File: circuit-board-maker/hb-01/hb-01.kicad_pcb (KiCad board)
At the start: 2 copper layers, 48 x 40 mm, 0 parts

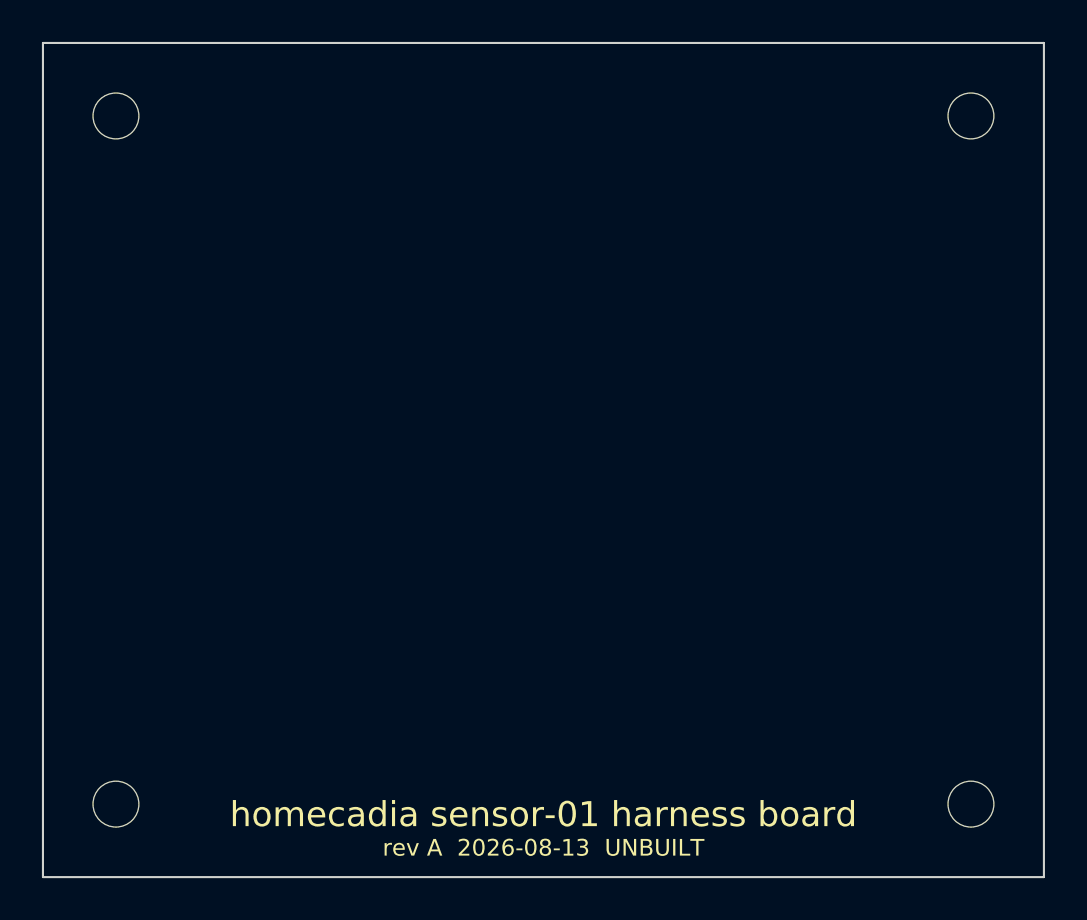
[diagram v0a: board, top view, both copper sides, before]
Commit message: fix(pcb): validate both boards against KiCad 10, place footprints, fix real errors
Ran the generated files through the Windows KiCad 10.0.5 install via
kicad-cli from WSL. This turned the boards from unvalidated text into
something KiCad parses, places, DRCs and renders - and caught six real
errors in the process.

Verified:
- all 13 footprint library refs resolve against KiCad 10's libraries
- kicad-cli pcb upgrade accepts both boards
- 26 footprints place with nets assigned, 0 missing
- J1's 17 pads are byte-identical to the library after round-trip
- both boards render in 3D (img/*-render.png are kicad-cli output)
- sb-01 passes DRC with 0 errors
- encoder terminals checked against the Bourns PEC11R datasheet:
  5x dia-1.0mm holes, 2.5mm pitch, 5.0mm spans - footprint matches

Fixed:
- Sensirion_DFN-4-1EP_1.5x1.5mm_P0.8mm_EP0.7x0.9mm does not exist. The
  real footprint is Sensirion_DFN-4_1.5x1.5mm_P0.8mm_SHT4x_NoCentralPad
- encoder moved from the Alps EC11E footprint to Bourns
  PEC12R-3x17F-Sxxxx; identical pad coordinates but 3.1mm oval boss
  holes instead of 2.8mm round, which is the safer error direction
- USB-C on hb-01 and JST-SH on sb-01 both hung off the board edge
- sb-01 C1 and J1 collided; board grown 12x12 -> 14x16 and reprovisioned
- sb-01 silkscreen overflowed the board outline
- D+/D- were documented as broken out to test pads but never netted;
  they now go to TP5/TP6

Not resolved, documented in README: hb-01 reports 65 DRC errors, all 65
inside J1 and none anywhere else. The XKB USB-C land pattern has 0.2mm
pad gaps and kicad-cli falls back to KiCad's default 0.2mm clearance
because this hand-written .kicad_pro is too minimal to load rules from -
setting the netclass to 0.05mm changed nothing. Needs one pass through
Board Setup in the GUI. That is where these generator scripts stop.

Also gitignores .kicad_prl, which is per-user local state.
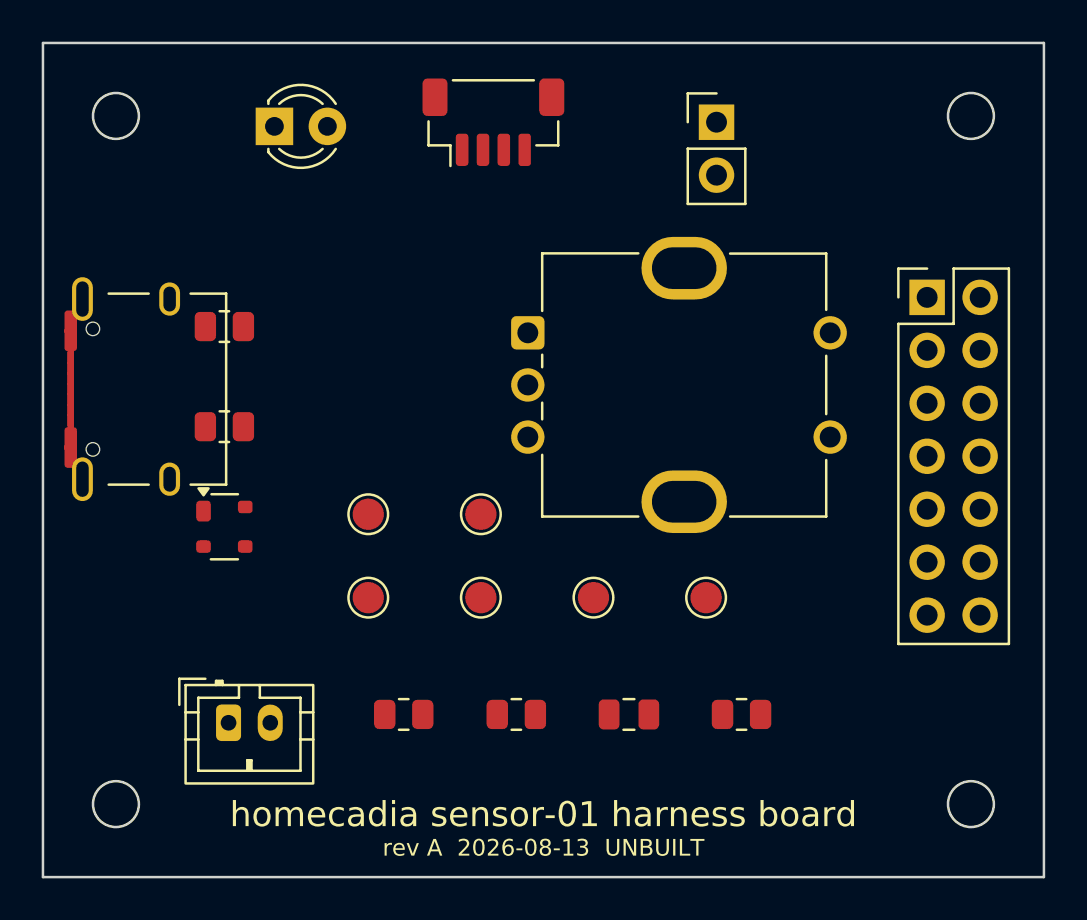
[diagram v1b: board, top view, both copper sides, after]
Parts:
- added C1: 100nF, Capacitor_SMD:C_0805_2012Metric, F.Cu at (28.1, 32.2)
- added D1: SP0503BAHTG, Package_TO_SOT_SMD:SOT-143, F.Cu at (8.70, 23.2)
- added D2: LED 3mm, LED_THT:LED_D3.0mm, F.Cu at (11.1, 4.00)
- added H1: M2, MountingHole:MountingHole_2.2mm_M2, F.Cu at (3.50, 3.50)
- added H2: M2, MountingHole:MountingHole_2.2mm_M2, F.Cu at (44.5, 3.50)
- added H3: M2, MountingHole:MountingHole_2.2mm_M2, F.Cu at (3.50, 36.5)
- added H4: M2, MountingHole:MountingHole_2.2mm_M2, F.Cu at (44.5, 36.5)
- added J1: USB-C 16P, Connector_USB:USB_C_Receptacle_XKB_U262-16XN-4BVC11, F.Cu at (5.00, 16.6)
- added J2: XIAO field 2x7, Connector_PinHeader_2.54mm:PinHeader_2x07_P2.54mm_Vertical, F.Cu at (42.4, 12.2)
- added J3: BAT JST-PH, Connector_JST:JST_PH_B2B-PH-K_1x02_P2.00mm_Vertical, F.Cu at (8.90, 32.6)
- added J4: SHT40 JST-SH, Connector_JST:JST_SH_BM04B-SRSS-TB_1x04-1MP_P1.00mm_Vertical, F.Cu at (21.6, 3.80)
- added J5: 5V out, Connector_PinHeader_2.54mm:PinHeader_1x02_P2.54mm_Vertical, F.Cu at (32.3, 3.80)
- added R1: 5.1k, Resistor_SMD:R_0805_2012Metric, F.Cu at (8.70, 13.6)
- added R2: 5.1k, Resistor_SMD:R_0805_2012Metric, F.Cu at (8.70, 18.4)
- added R3: 1M 1%, Resistor_SMD:R_0805_2012Metric, F.Cu at (17.3, 32.2)
- added R4: 1M 1%, Resistor_SMD:R_0805_2012Metric, F.Cu at (22.7, 32.2)
- added R5: 1k, Resistor_SMD:R_0805_2012Metric, F.Cu at (33.5, 32.2)
- added SW1: PEC11R-4220F-S0024, Rotary_Encoder:RotaryEncoder_Bourns_Vertical_PEC12R-3x17F-Sxxxx, F.Cu at (23.2, 13.9)
- added TP1: VBAT, TestPoint:TestPoint_Pad_D1.5mm, F.Cu at (15.6, 26.6)
- added TP2: VDIV, TestPoint:TestPoint_Pad_D1.5mm, F.Cu at (21.0, 26.6)
- added TP3: GND, TestPoint:TestPoint_Pad_D1.5mm, F.Cu at (26.4, 26.6)
- added TP4: 3V3, TestPoint:TestPoint_Pad_D1.5mm, F.Cu at (31.8, 26.6)
- added TP5: USB_DP, TestPoint:TestPoint_Pad_D1.5mm, F.Cu at (15.6, 22.6)
- added TP6: USB_DM, TestPoint:TestPoint_Pad_D1.5mm, F.Cu at (21.0, 22.6)
